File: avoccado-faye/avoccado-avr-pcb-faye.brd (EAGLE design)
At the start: 25 x 24.5 mm, 51 parts, among them Q1 16MHz, Q2 FET, U2 MCP73831

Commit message: Initial commit for Avoccado° Faye
new: battery voltage sensing
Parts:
- added C7: 0.1uF, SparkFun:C0402
- added R7, R8: 1M, SparkFun-Resistors:0603-RES
- moved C3 1.00 mm to (20.8, 16.2), turned to 270 degrees
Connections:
- new net N$3: C7.1, R7.2, R8.1
- net GND: now also C7.2, R7.1
- net VBAT: now also R8.2
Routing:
- net GND: track 126.8 -> 117.4 mm, vias 6 -> 5
- net 3.3V: track 83.4 -> 77.1 mm
- net D2: track 19.6 -> 20.6 mm

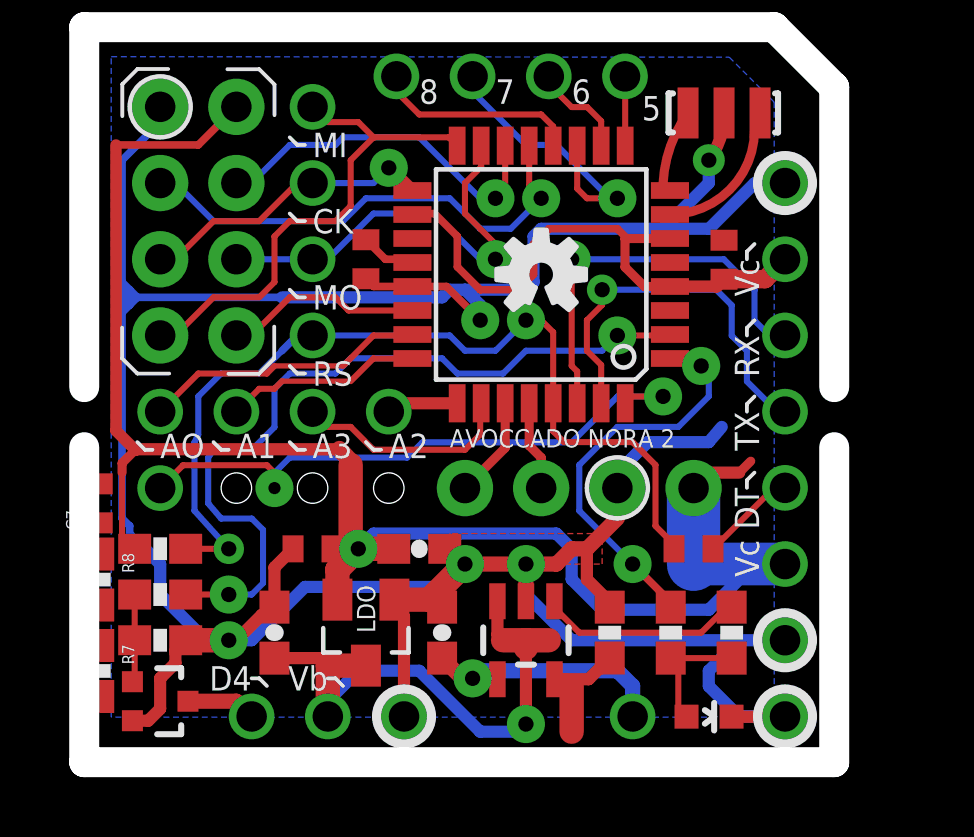
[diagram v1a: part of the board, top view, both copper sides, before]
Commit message: ditching not connected pins from MPU board
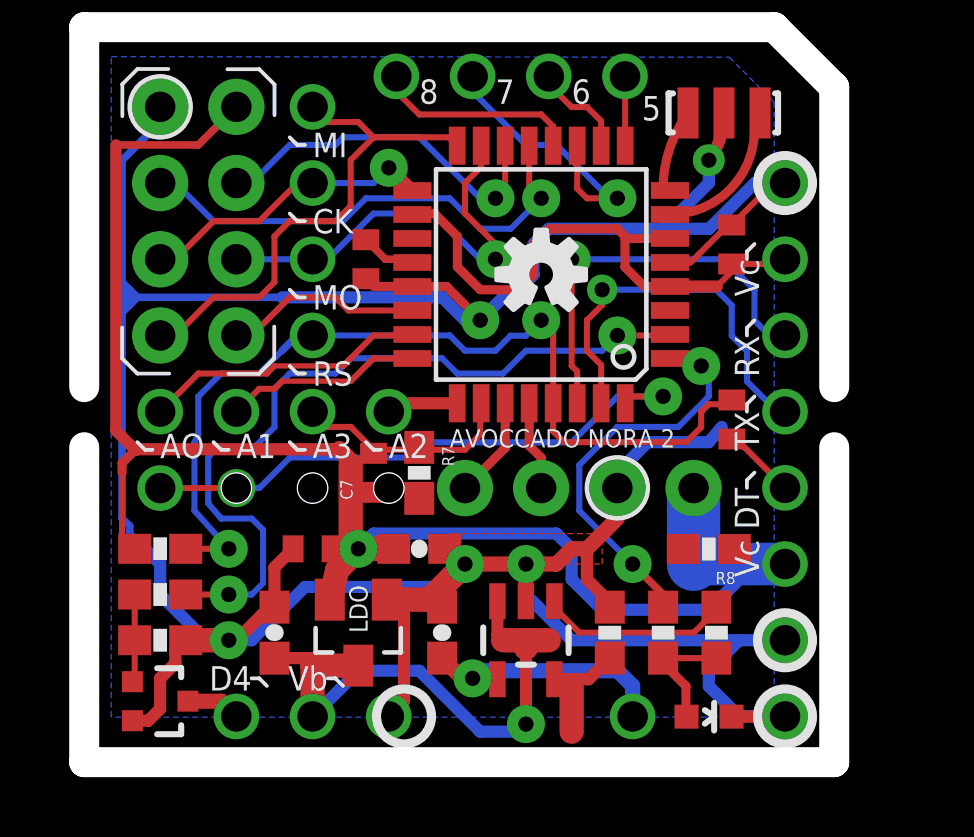
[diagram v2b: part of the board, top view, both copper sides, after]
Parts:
- moved R8 20.3 mm to (20.3, 6.60), turned to 180 degrees
- moved R7 12.5 mm to (10.7, 9.14)
- moved C7 9.20 mm to (9.14, 9.14)
- moved C2 4.50 mm to (21.1, 10.9), turned to 270 degrees
- moved C3 0.57 mm to (21.1, 16.8)
- moved JP25 0.51 mm to (9.65, 1.02)
- moved JP23 0.51 mm to (4.57, 1.02)
- moved JP24 0.51 mm to (7.11, 1.02)
- moved R4 0.51 mm to (20.6, 3.82)
- moved LDO 0.25 mm to (8.64, 3.82)
- moved R6 0.25 mm to (18.8, 3.82)
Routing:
- net GND: track 117.4 -> 121.9 mm
- net 3.3V: track 77.1 -> 75.0 mm
- net D2: track 20.6 -> 19.4 mm
- net DTR: track 3.24 -> 2.45 mm
- net VIBR: track 2.33 -> 1.83 mm

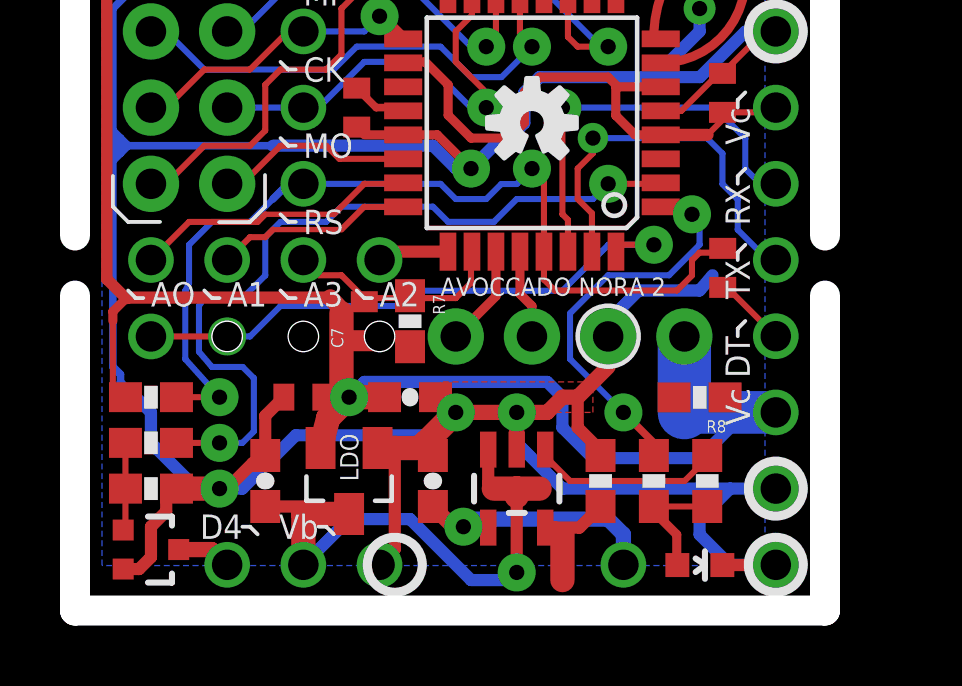
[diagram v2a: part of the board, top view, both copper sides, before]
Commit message: redesign lower half of Faye
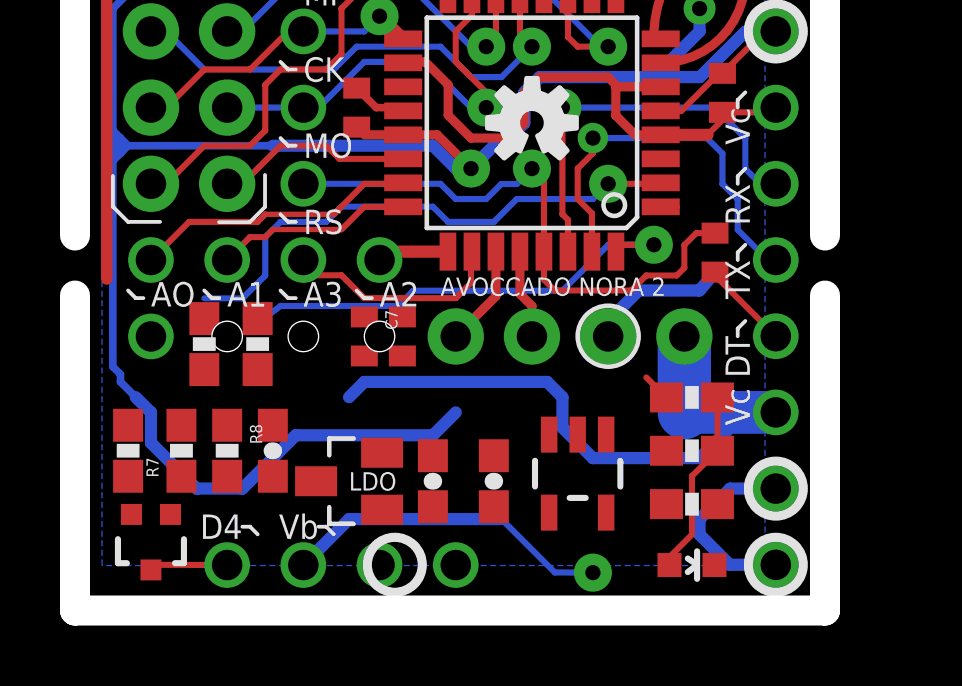
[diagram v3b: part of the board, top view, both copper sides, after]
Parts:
- moved R8 15.8 mm to (4.57, 4.83), turned to 270 degrees
- moved R7 8.76 mm to (3.05, 4.83), turned to 90 degrees
- moved JP17 5.59 mm to (12.2, 1.02)
- moved R2 3.97 mm to (5.59, 8.38), turned to 270 degrees
- moved C10 3.87 mm to (10.4, 8.64), turned to 90 degrees
- moved R1 3.74 mm to (3.81, 8.38), turned to 270 degrees
- moved R3 3.14 mm to (20.1, 3.05), turned to 180 degrees
- moved R6 3.06 mm to (20.1, 6.60), turned to 0 degrees
- moved C6 2.90 mm to (11.4, 3.81), turned to 270 degrees
- moved U2 2.09 mm to (16.3, 4.06)
- moved C4 2.03 mm to (13.5, 3.81)
- moved R5 1.47 mm to (1.27, 4.83), turned to 90 degrees
- moved R4 1.13 mm to (20.1, 4.83), turned to 180 degrees
- moved C5 1.04 mm to (6.10, 4.83)
- moved C2 0.57 mm to (20.8, 11.4)
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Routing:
- net GND: track 121.9 -> 80.8 mm, vias 5 -> 2
- net 3.3V: track 75.0 -> 55.9 mm, vias 1 -> 0
- net D3: track 14.2 -> 2.45 mm, vias 2 -> 0
- net RESET: track 30.7 -> 19.2 mm, vias 2 -> 1
- net 5V: track 8.95 -> 0.00 mm, vias 1 -> 0
- net D4: track 26.5 -> 18.0 mm, vias 2 -> 1
- net VBAT: track 19.5 -> 11.0 mm
- net SOC: track 6.71 -> 0.00 mm
- net CHG-PROG: track 4.33 -> 0.00 mm
- net D2: track 19.4 -> 15.9 mm, vias 2 -> 1
- net N$6: track 2.94 -> 0.17 mm
- net LED: track 4.05 -> 6.49 mm
- net VIBR: track 1.83 -> 2.61 mm
- net DTR: track 2.45 -> 3.15 mm
- removed copper zone on layer 1, net GND

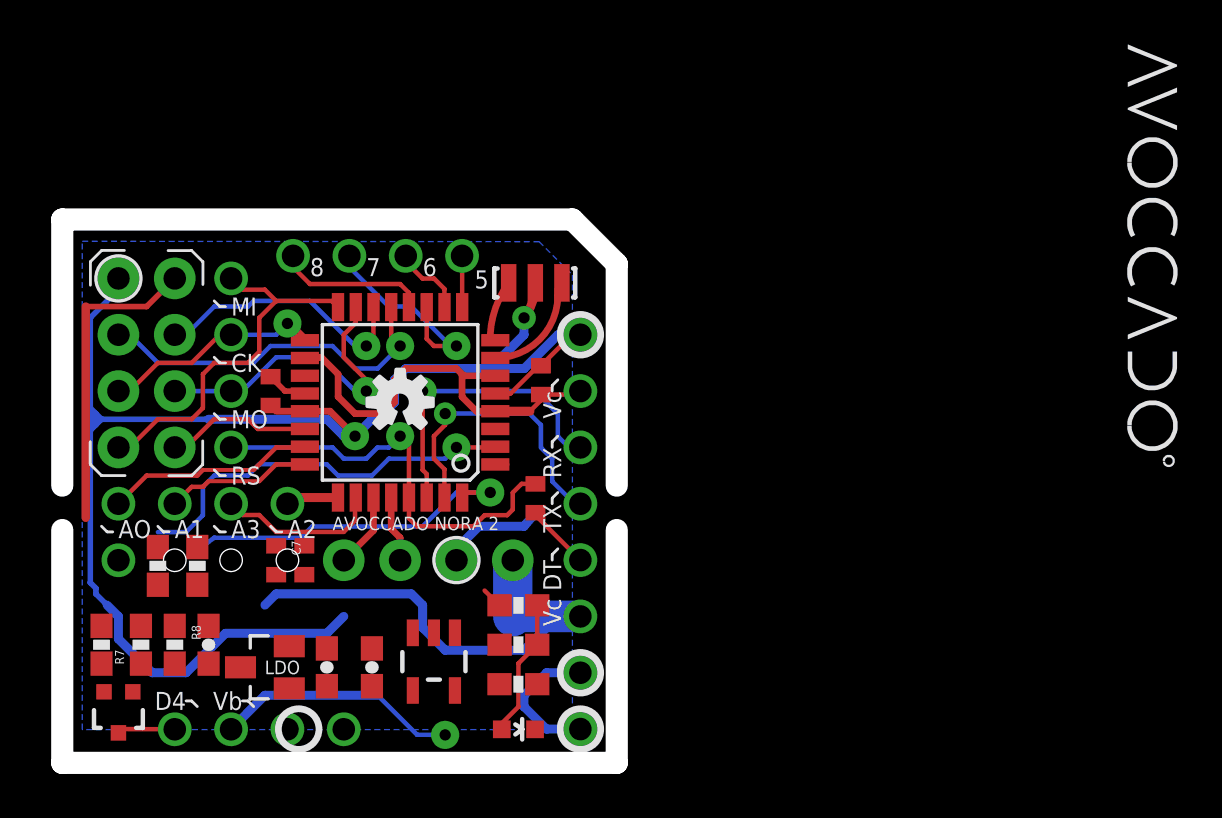
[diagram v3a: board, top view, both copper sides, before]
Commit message: rerouting bottom half
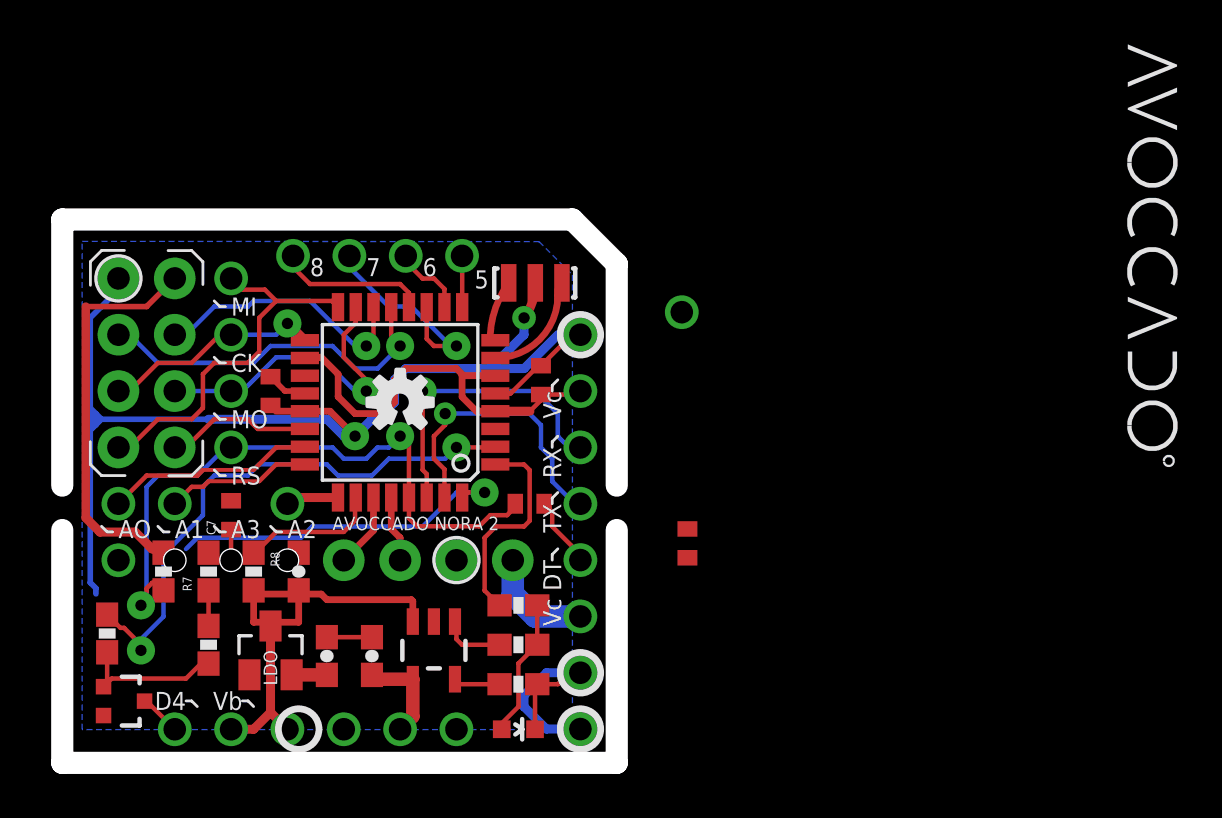
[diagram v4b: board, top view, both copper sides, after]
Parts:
- added JP1, JP7: M01NOSILK-KIT, SparkFun-Connectors:1X01NS-KIT
- moved JP22 22.1 mm to (27.4, 19.8)
- moved C10 17.3 mm to (27.7, 9.40), turned to 270 degrees
- moved C5 5.24 mm to (10.2, 8.13)
- moved R8 4.85 mm to (8.13, 8.13)
- moved R5 4.83 mm to (6.10, 4.83), turned to 270 degrees
- moved R7 4.49 mm to (6.10, 8.13)
- moved R1 3.81 mm to (1.52, 5.33)
- moved C7 2.87 mm to (7.11, 10.7), turned to 90 degrees
- moved JP25 2.54 mm to (12.2, 1.02)
- moved JP17 2.54 mm to (14.7, 1.02)
- moved R2 1.55 mm to (4.06, 8.13), turned to 90 degrees
- moved LDO 0.80 mm to (8.89, 4.57), turned to 0 degrees
- moved Q2 0.57 mm to (2.29, 2.29), turned to 270 degrees
- moved U2 0.51 mm to (16.3, 4.57)
- moved C4 0.51 mm to (13.5, 4.32)
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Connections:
- removed net N$3: C7.1, R7.2, R8.1
- net A3: now also C7.1, R7.2, R8.1
- net GND: now also JP7.1
- net VBAT: now also JP1.1
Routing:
- net 3.3V: track 55.9 -> 44.0 mm
- net GND: track 80.8 -> 69.8 mm
- net RESET: track 19.2 -> 29.6 mm, vias 1 -> 2
- net VBAT: track 11.0 -> 20.3 mm, vias 1 -> 0
- net D3: track 2.45 -> 11.1 mm
- net D4: track 18.0 -> 25.2 mm, vias 1 -> 2
- net N$6: track 0.17 -> 6.78 mm
- net 5V: track 0.00 -> 4.42 mm
- net SOC: track 0.00 -> 2.87 mm
- net A3: track 7.38 -> 9.99 mm
- net CHG-PROG: track 0.00 -> 2.10 mm
- net VIBR: track 2.61 -> 1.89 mm

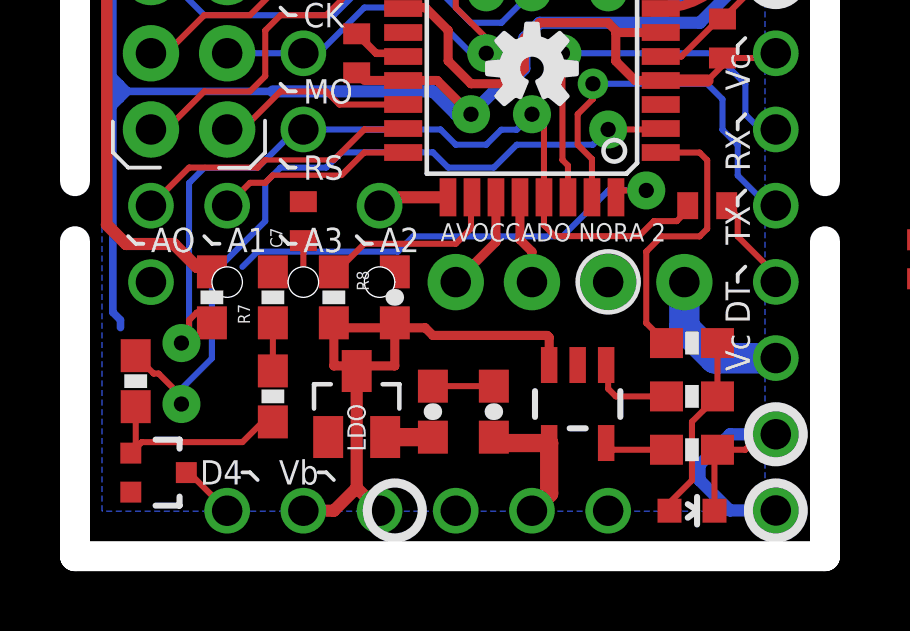
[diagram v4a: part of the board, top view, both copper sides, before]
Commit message: rerouting bottom half WIP
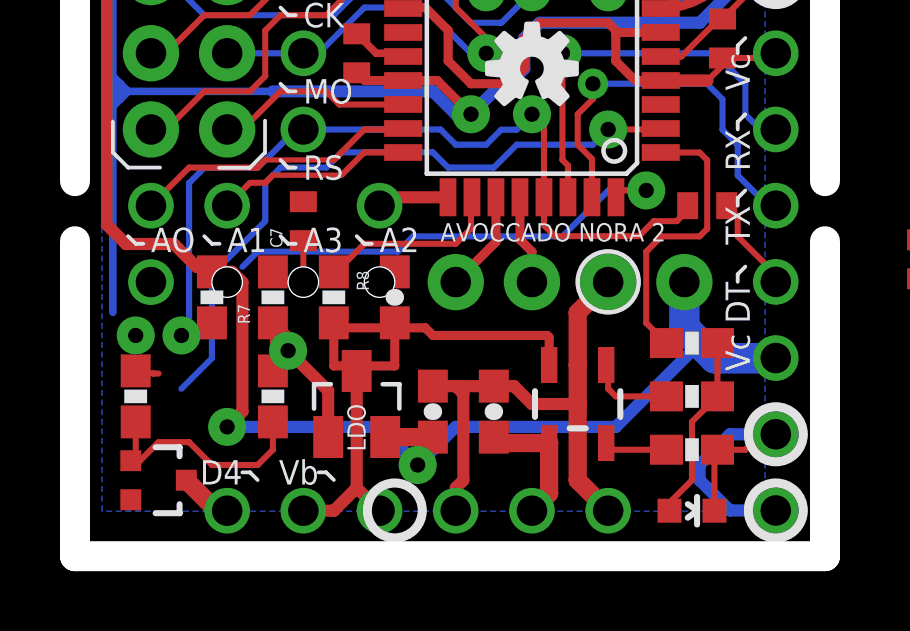
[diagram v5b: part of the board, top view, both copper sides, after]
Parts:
- moved R1 0.51 mm to (1.52, 4.83)
- moved Q2 0.25 mm to (2.29, 2.03)
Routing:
- net 3.3V: track 44.0 -> 69.3 mm, vias 0 -> 2
- net GND: track 69.8 -> 89.7 mm, vias 2 -> 3
- net D4: track 25.2 -> 23.1 mm
- net N$6: track 6.78 -> 8.29 mm
- net RESET: track 29.6 -> 28.9 mm

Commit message: bottom WIP
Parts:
- moved JP22 22.1 mm to (7.11, 11.2)
- moved C5 6.53 mm to (16.5, 6.60), turned to 0 degrees
- moved C7 3.25 mm to (9.65, 8.64), turned to 270 degrees
- moved U2 0.80 mm to (16.5, 3.81)
- moved R7 0.51 mm to (6.10, 8.64)
- moved R8 0.51 mm to (8.13, 8.64)
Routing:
- net GND: track 89.7 -> 102.1 mm
- net D2: track 15.6 -> 25.7 mm, vias 1 -> 2
- net N$6: track 8.29 -> 5.93 mm
- net VBAT: track 20.3 -> 18.7 mm
- net 3.3V: track 69.3 -> 68.3 mm
- net D4: track 23.1 -> 24.1 mm
- net SOC: track 2.87 -> 2.01 mm
- net A3: track 9.99 -> 10.8 mm

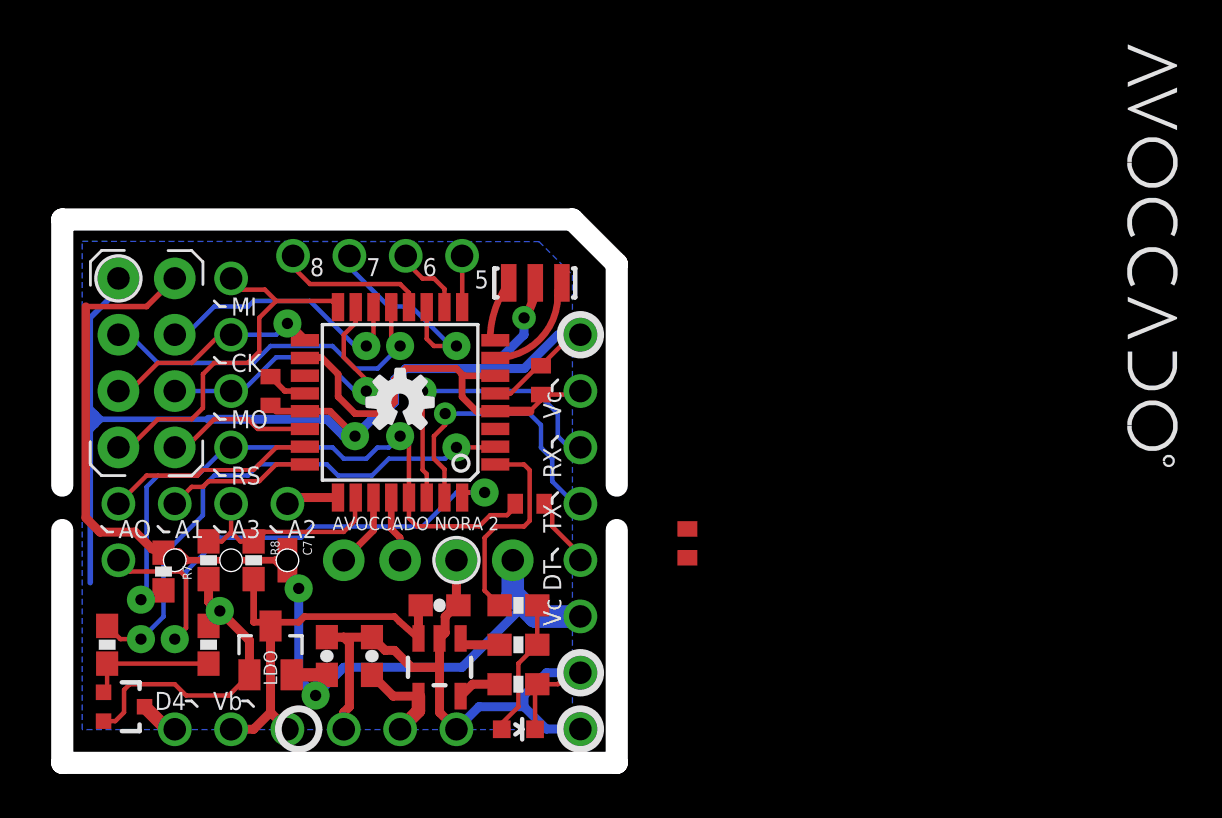
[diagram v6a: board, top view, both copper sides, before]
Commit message: reroute filter C top right
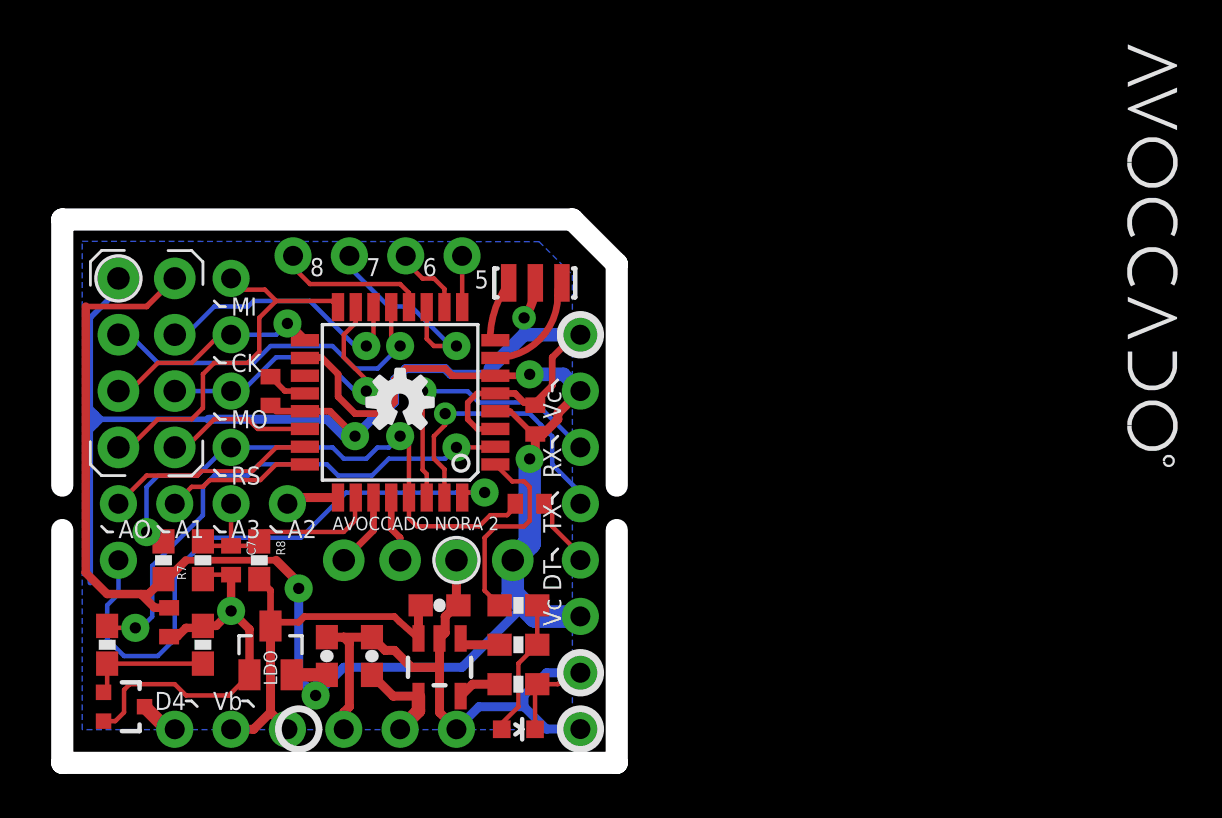
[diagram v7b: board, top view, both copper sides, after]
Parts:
- moved C10 23.6 mm to (4.32, 5.84)
- moved C7 2.54 mm to (7.11, 8.64)
- moved C3 1.80 mm to (20.8, 15.0)
- moved R2 0.51 mm to (4.06, 8.64), turned to 270 degrees
- moved R5 0.25 mm to (5.84, 4.83)
- moved R7 0.25 mm to (5.84, 8.64)
- moved R8 0.25 mm to (8.38, 8.64)
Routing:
- net 3.3V: track 68.3 -> 80.7 mm, vias 2 -> 4
- net GND: track 102.1 -> 108.6 mm
- net RESET: track 28.9 -> 25.1 mm
- net D2: track 25.7 -> 27.0 mm, vias 2 -> 1
- net D3: track 11.1 -> 10.1 mm
- net D4: track 24.1 -> 23.4 mm
- net RXI: track 13.6 -> 13.1 mm
